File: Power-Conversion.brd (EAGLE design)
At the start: 160 x 81.3 mm, 41 parts

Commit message: closer connectors
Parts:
- moved F2 125.5 mm to (45.7, 63.5), turned to 180 degrees
- moved F7 119.5 mm to (45.7, 6.35), turned to 180 degrees
- moved F5 116.6 mm to (45.7, 29.2), turned to 180 degrees
- moved F1 115.3 mm to (45.7, 74.9), turned to 180 degrees
- moved F6 97.9 mm to (45.7, 17.8), turned to 180 degrees
- moved F4 94.6 mm to (45.7, 40.6), turned to 180 degrees
- moved F3 72.7 mm to (45.7, 52.1), turned to 180 degrees
- moved U$3 12.7 mm to (114.3, 33.0)
- moved U$2 5.08 mm to (114.3, 55.9)
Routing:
- added copper zone on layer 1, net N$11

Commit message: saturday
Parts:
- moved R1 181.1 mm to (96.5, 39.4), turned to 270 degrees
- moved R2 174.1 mm to (85.1, 39.4)
- moved U$5 172.6 mm to (96.5, 43.2)
- moved U$6 170.6 mm to (88.9, 39.4), turned to 90 degrees
- moved U$4 167.1 mm to (92.7, 39.4), turned to 90 degrees
- moved V-_ESC3 137.5 mm to (50.8, 38.1)
- moved U$7 126.1 mm to (87.6, 44.5), turned to 90 degrees
- moved V-_ESC2 121.6 mm to (39.4, 38.1)
- moved V-_ESC1 118.2 mm to (45.7, 45.7)
- moved I2C_ESC5 113.3 mm to (54.6, 31.8), turned to 90 degrees
- moved I2C_ESC3 113.0 mm to (30.5, 49.5), turned to 90 degrees
- moved I2C_ESC6 111.4 mm to (43.2, 31.8), turned to 90 degrees
- moved V+_ESC5 110.3 mm to (50.8, 27.9)
- moved I2C_ESC7 109.6 mm to (31.8, 31.8), turned to 90 degrees
- moved I2C_ESC8 107.8 mm to (20.3, 31.8), turned to 90 degrees
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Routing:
- net SDA: track 0.00 -> 95.3 mm
- net SCL: track 0.00 -> 95.3 mm
- net V+: track 0.00 -> 31.4 mm
- net V-: track 0.00 -> 28.8 mm
- net ONOFF: track 0.00 -> 27.2 mm
- net N$10: track 0.00 -> 7.11 mm
- net N$9: track 0.00 -> 2.10 mm
- added copper zone on layer 1, net N$1
- added copper zone on layer 1, net N$2
- added copper zone on layer 1, net N$3
- added copper zone on layer 1, net N$4
- added copper zone on layer 1, net N$5
- added copper zone on layer 1, net N$6
- added copper zone on layer 1, net N$7
- added copper zone on layer 1, net N$8
- removed copper zone on layer 1, net N$11

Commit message: Fuse and prelim MCU connections
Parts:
- removed F4, F6, F8: (no value), MotherboardParts:KEYSTONE_FUSE_3587
- added C1, C2: 0.1uF, SparkFun-Capacitors:0603-CAP
- added I2C_ESC10, I2C_ESC9: (no value), SparkFun-Connectors:1X02
- added R3: 10K, SparkFun-Resistors:0603-RES
- added U1: ATMEGA328P_TQFP, SparkFun-DigitalIC:TQFP32-08
- added U2: LM1085IS-3.3, PowerComponents:TO254P1435X457-3N
- added V+_ESC10, V+_ESC9, V-_ESC10, V-_ESC9: (no value), SparkFun-Connectors:BANANA_CONN
- moved F2 189.8 mm to (36.1, -120.9), turned to 0 degrees
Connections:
- removed net N$2: F2.P$3, F2.P$4, V+_ESC2.P$1
- removed net N$4: F4.P$3, F4.P$4, V+_ESC4.P$1
- removed net N$6: F6.P$3, F6.P$4, V+_ESC6.P$1
- removed net N$8: F8.P$3, F8.P$4, V+_ESC8.P$1
- new net +5V: C1.1, C2.1, R3.1, U1.18, U1.20, U1.4, U1.6, U2.2, U2.4
- new net N$11: F2.P$3, F2.P$4, V+_ESC10.P$1, V+_ESC9.P$1
- new net N$13: R3.2, U1.29
- net GND: now also C1.2, C2.2, U1.21, U1.3, U1.5, U2.1, V-_ESC10.P$1, V-_ESC9.P$1
- net N$1: now also V+_ESC2.P$1
- net N$3: now also V+_ESC4.P$1
- net N$5: now also V+_ESC6.P$1
- net N$7: now also V+_ESC8.P$1
- net SCL: now also U1.28; no longer I2C_ESC1.1, I2C_ESC2.1, I2C_ESC3.1, I2C_ESC4.1, I2C_ESC5.1, I2C_ESC6.1, I2C_ESC7.1, I2C_ESC8.1
- net SDA: now also U1.27; no longer I2C_ESC1.2, I2C_ESC2.2, I2C_ESC3.2, I2C_ESC4.2, I2C_ESC5.2, I2C_ESC6.2, I2C_ESC7.2, I2C_ESC8.2
- net VCC: now also U2.3; no longer F4.P$1, F4.P$2, F6.P$1, F6.P$2, F8.P$1, F8.P$2
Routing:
- net SDA: track 95.3 -> 0.00 mm
- net SCL: track 95.3 -> 0.00 mm

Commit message: Placement and early routing of AVR board
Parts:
- added C3: 0.1uF, SparkFun-Capacitors:0603-CAP
- added J1: AVR_SPI_PRG_6PTH, SparkFun-Connectors:2X3
- added R4: 1K, SparkFun-Resistors:0603-RES
- added R5, R6: 470, SparkFun-Resistors:0603-RES
- added U$8: TLC59401PWPR, MotherboardParts:TLC59401PWPR
- I2C_ESC1, I2C_ESC10, I2C_ESC2, I2C_ESC3, I2C_ESC4, I2C_ESC5, I2C_ESC6, I2C_ESC7, I2C_ESC8, I2C_ESC9: device SparkFun-Connectors:1X02 -> SparkFun-Connectors:1X01
- moved C2 202.5 mm to (4.70, 38.9)
- moved C1 201.1 mm to (4.70, 40.5)
- moved R3 198.3 mm to (10.3, 39.8), turned to 90 degrees
- moved I2C_ESC10 193.8 mm to (14.0, 71.1)
- moved F2 188.8 mm to (50.8, 67.3), turned to 180 degrees
- moved I2C_ESC9 187.3 mm to (14.0, 63.5)
- moved U1 174.0 mm to (5.97, 46.5), turned to 270 degrees
- moved U2 170.9 mm to (6.35, 29.7)
- moved V-_ESC10 162.5 mm to (24.1, 71.1)
- moved V-_ESC9 149.5 mm to (19.1, 63.5)
- moved V+_ESC10 106.8 mm to (35.6, 71.1)
- moved V+_ESC9 96.2 mm to (27.9, 63.5)
- moved F1 63.8 mm to (50.8, 16.5), turned to 180 degrees
- moved F7 46.9 mm to (50.8, 54.6), turned to 180 degrees
- moved V+_ESC1 46.2 mm to (27.9, 12.7)
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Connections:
- new net GSCLK: U$8.P$25, U1.13
- new net N$12: R5.1, U$8.P$4
- new net N$14: R6.1, U$8.P$5
- new net N$15: I2C_ESC1.1, U$8.P$7
- new net N$16: I2C_ESC2.1, U$8.P$8
- new net N$17: I2C_ESC3.1, U$8.P$9
- new net N$18: I2C_ESC4.1, U$8.P$10
- new net N$19: I2C_ESC5.1, U$8.P$11
- new net N$20: I2C_ESC6.1, U$8.P$12
- new net N$21: I2C_ESC7.1, U$8.P$13
- new net N$22: I2C_ESC8.1, U$8.P$14
- new net N$23: I2C_ESC9.1, U$8.P$15
- new net N$24: I2C_ESC10.1, U$8.P$16
- new net N$25: R4.2, U$8.P$27
- new net N$26: J1.4, R6.2, U1.15
- new net N$27: U$8.P$2, U1.11
- new net N$29: J1.1, U1.16
- new net N$31: J1.3, R5.2, U1.17
- net +5V: now also C3.1, J1.2, U$8.P$26, U$8.P$28
- net GND: now also C3.2, J1.6, R4.1, U$8.P$1, U$8.P$6
- net N$13: now also J1.5, U$8.P$3
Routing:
- net +5V: track 0.00 -> 76.8 mm
- net N$20: track 0.00 -> 13.9 mm
- net GND: track 0.00 -> 11.4 mm, vias 0 -> 4
- net N$24: track 0.00 -> 9.03 mm
- net N$21: track 0.00 -> 8.52 mm
- net N$13: track 0.00 -> 7.74 mm
- net N$22: track 0.00 -> 2.97 mm
- net N$23: track 0.00 -> 2.76 mm
- net N$25: track 0.00 -> 2.01 mm
- net N$12: track 0.00 -> 1.72 mm
- net N$14: track 0.00 -> 1.70 mm
- added copper zone on layer 1, net +5V
- added copper zone on layer 1, net N$11
- removed copper zone on layer 1, net N$2
- removed copper zone on layer 1, net N$4
- removed copper zone on layer 1, net N$6
- removed copper zone on layer 1, net N$8

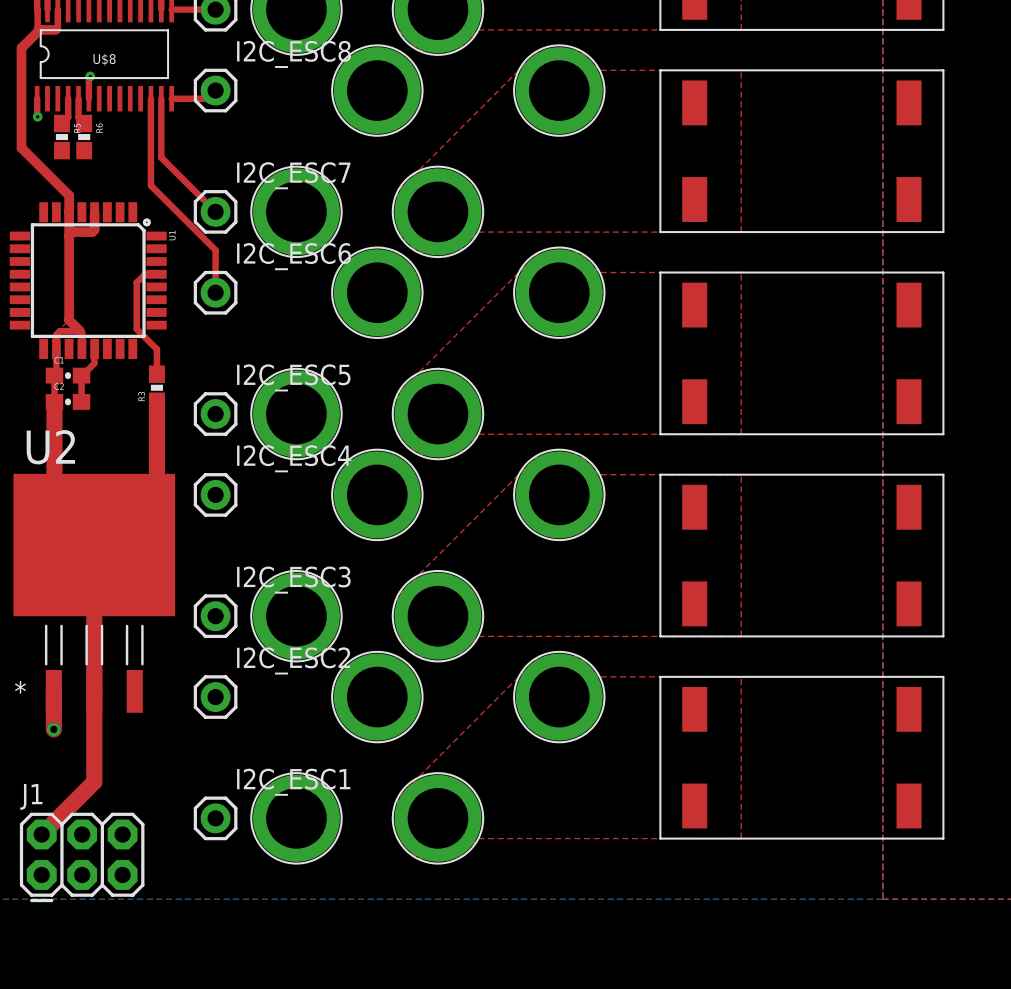
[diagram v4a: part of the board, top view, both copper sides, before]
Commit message: pwm routing
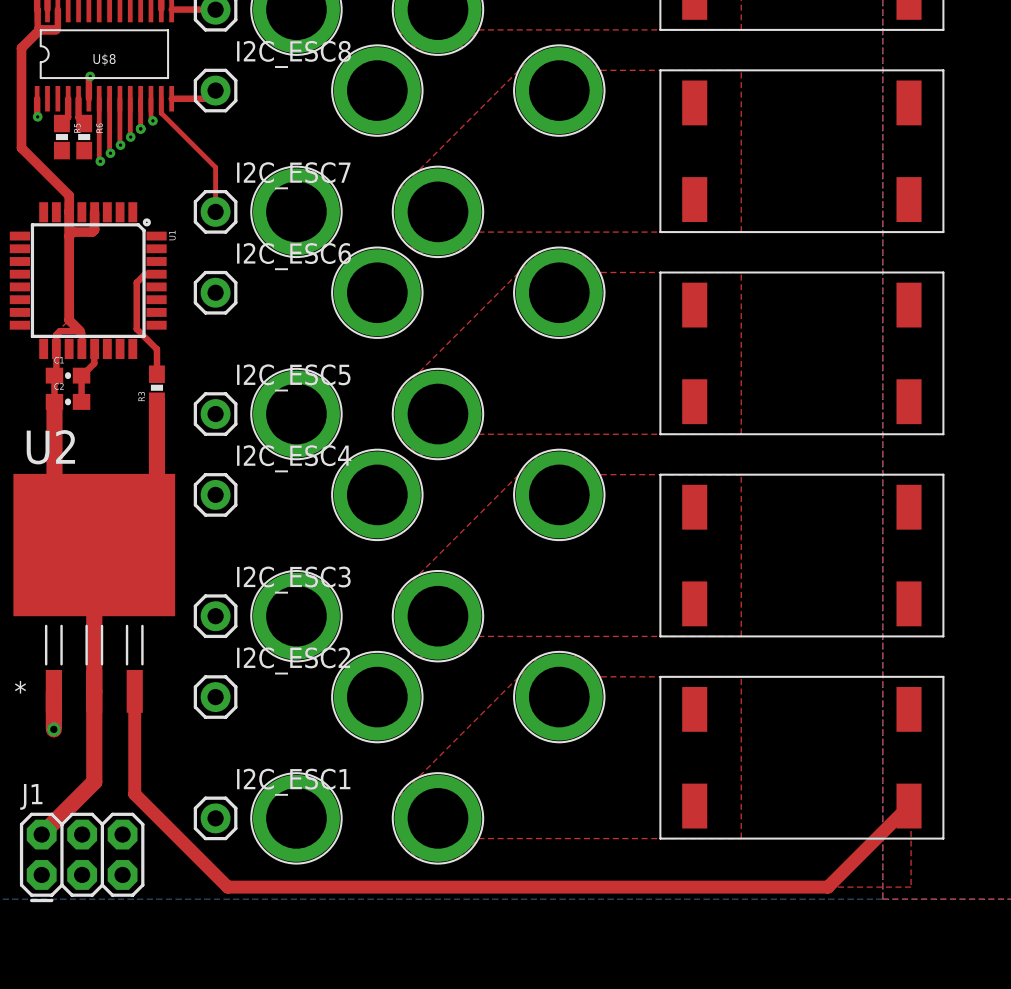
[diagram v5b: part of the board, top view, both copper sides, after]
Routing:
- net VCC: track 0.00 -> 59.6 mm
- net N$15: track 0.00 -> 48.2 mm, vias 0 -> 1
- net N$16: track 0.00 -> 40.3 mm, vias 0 -> 1
- net N$17: track 0.00 -> 35.0 mm, vias 0 -> 1
- net N$18: track 0.00 -> 27.1 mm, vias 0 -> 1
- net N$19: track 0.00 -> 21.8 mm, vias 0 -> 2
- net N$20: vias 0 -> 1
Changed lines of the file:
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@@
 <setting verticaltext="up"/>
 </settings>
-<grid distance="1" unitdist="mil" unit="mil" style="dots" multiple="1" display="no" altdistance="0.025" altunitdist="inch" altunit="inch"/>
+<grid distance="10" unitdist="mil" unit="mil" style="dots" multiple="1" display="yes" altdistance="0.025" altunitdist="inch" altunit="inch"/>
 <layers>
 <layer number="1" name="Top" color="4" fill="1" visible="yes" active="yes"/>
@@
 <layer number="14" name="Route14" color="1" fill="6" visible="yes" active="yes"/>
 <layer number="15" name="Route15" color="4" fill="6" visible="yes" active="yes"/>
-<layer number="16" name="Bottom" color="1" fill="1" visible="yes" active="yes"/>
+<layer number="16" name="Bottom" color="1" fill="1" visible="no" active="yes"/>
 <layer number="17" name="Pads" color="2" fill="1" visible="yes" active="yes"/>
 <layer number="18" name="Vias" color="2" fill="1" visible="yes" active="yes"/>
@@
 <contactref element="F2" pad="P$2"/>
 <contactref element="U2" pad="3"/>
-<wire x1="57.531" y1="19.5453" x2="8.89" y2="20.6756" width="0" layer="19" extent="1-1"/>
+<wire x1="8.89" y1="20.6756" x2="8.89" y2="14.224" width="0.8128" layer="1"/>
+<wire x1="8.89" y1="14.224" x2="14.732" y2="8.382" width="0.8128" layer="1"/>
+<wire x1="14.732" y1="8.382" x2="52.4383" y2="8.382" width="0.8128" layer="1"/>
+<wire x1="52.4383" y1="8.382" x2="57.531" y2="13.4747" width="0.8128" layer="1"/>
+<polygon width="0.4064" layer="1">
+<vertex x="52.324" y="8.382"/>
+<vertex x="57.658" y="13.716"/>
+<vertex x="57.658" y="8.382"/>
+</polygon>
 </signal>
 <signal name="GND">
@@
 <contactref element="U$8" pad="P$7"/>
 <contactref element="I2C_ESC1" pad="1"/>
-<wire x1="13.97" y1="12.7" x2="6.66" y2="57.906" width="0" layer="19" extent="1-1"/>
+<via x="6.731" y="53.975" extent="1-16" drill="0.2032" diameter="0.4572"/>
+<wire x1="6.66" y1="57.906" x2="6.66" y2="54.046" width="0.3048" layer="1"/>
+<wire x1="6.66" y1="54.046" x2="6.731" y2="53.975" width="0.3048" layer="1"/>
+<wire x1="6.731" y1="53.975" x2="6.731" y2="53.848" width="0.3048" layer="2"/>
+<wire x1="6.731" y1="53.848" x2="7.62" y2="52.959" width="0.3048" layer="2"/>
+<wire x1="7.62" y1="52.959" x2="7.62" y2="19.05" width="0.3048" layer="2"/>
+<wire x1="7.62" y1="19.05" x2="13.97" y2="12.7" width="0.3048" layer="2"/>
 </signal>
 <signal name="N$16">
 <contactref element="U$8" pad="P$8"/>
 <contactref element="I2C_ESC2" pad="1"/>
-<wire x1="13.97" y1="20.32" x2="7.31" y2="57.906" width="0" layer="19" extent="1-1"/>
+<via x="7.366" y="54.483" extent="1-16" drill="0.2032" diameter="0.4572"/>
+<wire x1="7.31" y1="57.906" x2="7.31" y2="54.539" width="0.3048" layer="1"/>
+<wire x1="7.31" y1="54.539" x2="7.366" y2="54.483" width="0.3048" layer="1"/>
+<wire x1="7.366" y1="54.483" x2="7.366" y2="54.356" width="0.3048" layer="2"/>
+<wire x1="7.366" y1="54.356" x2="8.509" y2="53.213" width="0.3048" layer="2"/>
+<wire x1="8.509" y1="53.213" x2="8.509" y2="25.781" width="0.3048" layer="2"/>
+<wire x1="8.509" y1="25.781" x2="13.97" y2="20.32" width="0.3048" layer="2"/>
 </signal>
 <signal name="N$17">
 <contactref element="U$8" pad="P$9"/>
 <contactref element="I2C_ESC3" pad="1"/>
-<wire x1="13.97" y1="25.4" x2="7.96" y2="57.906" width="0" layer="19" extent="1-1"/>
+<via x="8.001" y="54.991" extent="1-16" drill="0.2032" diameter="0.4572"/>
+<wire x1="7.96" y1="57.906" x2="7.96" y2="55.032" width="0.3048" layer="1"/>
+<wire x1="7.96" y1="55.032" x2="8.001" y2="54.991" width="0.3048" layer="1"/>
+<wire x1="8.001" y1="54.991" x2="8.001" y2="54.864" width="0.3048" layer="2"/>
+<wire x1="8.001" y1="54.864" x2="9.271" y2="53.594" width="0.3048" layer="2"/>
+<wire x1="9.271" y1="53.594" x2="9.271" y2="30.099" width="0.3048" layer="2"/>
+<wire x1="9.271" y1="30.099" x2="13.97" y2="25.4" width="0.3048" layer="2"/>
 </signal>
 <signal name="N$18">
 <contactref element="U$8" pad="P$10"/>
 <contactref element="I2C_ESC4" pad="1"/>
-<wire x1="13.97" y1="33.02" x2="8.61" y2="57.906" width="0" layer="19" extent="1-1"/>
+<via x="8.636" y="55.499" extent="1-16" drill="0.2032" diameter="0.4572"/>
+<wire x1="8.61" y1="57.906" x2="8.61" y2="55.525" width="0.3048" layer="1"/>
+<wire x1="8.61" y1="55.525" x2="8.636" y2="55.499" width="0.3048" layer="1"/>
+<wire x1="8.636" y1="55.499" x2="10.287" y2="53.848" width="0.3048" layer="2"/>
+<wire x1="10.287" y1="53.848" x2="10.287" y2="36.703" width="0.3048" layer="2"/>
+<wire x1="10.287" y1="36.703" x2="13.97" y2="33.02" width="0.3048" layer="2"/>
 </signal>
 <signal name="N$19">
 <contactref element="U$8" pad="P$11"/>
 <contactref element="I2C_ESC5" pad="1"/>
-<wire x1="13.97" y1="38.1" x2="9.26" y2="57.906" width="0" layer="19" extent="1-1"/>
+<via x="9.271" y="56.007" extent="1-16" drill="0.2032" diameter="0.4572"/>
+<wire x1="9.26" y1="57.906" x2="9.26" y2="56.018" width="0.3048" layer="1"/>
+<wire x1="9.26" y1="56.018" x2="9.271" y2="56.007" width="0.3048" layer="1"/>
+<via x="9.26" y="56.018" extent="1-16" drill="0.2032" diameter="0.4572"/>
+<wire x1="9.26" y1="56.018" x2="11.303" y2="53.975" width="0.3048" layer="2"/>
+<wire x1="11.303" y1="53.975" x2="11.303" y2="40.767" width="0.3048" layer="2"/>
+<wire x1="11.303" y1="40.767" x2="13.97" y2="38.1" width="0.3048" layer="2"/>
 </signal>
 <signal name="N$20">
 <contactref element="U$8" pad="P$12"/>
 <contactref element="I2C_ESC6" pad="1"/>
-<wire x1="9.91" y1="57.906" x2="9.91" y2="52.447" width="0.4064" layer="1"/>
-<wire x1="13.97" y1="48.387" x2="13.97" y2="45.72" width="0.4064" layer="1"/>
-<wire x1="9.91" y1="52.447" x2="13.97" y2="48.387" width="0.4064" layer="1"/>
+<via x="10.033" y="56.515" extent="1-16" drill="0.2032" diameter="0.4572"/>
+<wire x1="9.91" y1="57.906" x2="9.91" y2="56.519" width="0.3048" layer="1"/>
+<wire x1="9.91" y1="56.519" x2="10.033" y2="56.515" width="0.3048" layer="1"/>
+<wire x1="10.033" y1="56.515" x2="10.033" y2="56.261" width="0.3048" layer="2"/>
+<wire x1="10.033" y1="56.261" x2="12.192" y2="54.102" width="0.3048" layer="2"/>
+<wire x1="12.192" y1="54.102" x2="12.192" y2="47.498" width="0.3048" layer="2"/>
+<wire x1="12.192" y1="47.498" x2="13.97" y2="45.72" width="0.3048" layer="2"/>
 </signal>
 <signal name="N$21">
 <contactref element="U$8" pad="P$13"/>
 <contactref element="I2C_ESC7" pad="1"/>
-<wire x1="10.56" y1="57.906" x2="10.56" y2="54.21" width="0.4064" layer="1"/>
-<wire x1="10.56" y1="54.21" x2="13.97" y2="50.8" width="0.4064" layer="1"/>
+<wire x1="10.56" y1="57.906" x2="10.56" y2="57.004" width="0.3048" layer="1"/>
+<wire x1="10.56" y1="57.004" x2="13.97" y2="53.594" width="0.3048" layer="1"/>
+<wire x1="13.97" y1="53.594" x2="13.97" y2="50.8" width="0.3048" layer="1"/>
 </signal>
 <signal name="N$22">
